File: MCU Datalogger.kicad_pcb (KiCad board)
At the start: 4 copper layers, 52.1 x 33 mm, 31 parts, among them J1 Conn_01x04_Pin, J2 Conn_01x09_Pin, J3 Conn_01x04_Pin, J4 Conn_02x03_Odd_Even, U1 DS1337S+, U2 24LC1025, U3 24LC1025, U4 ATMEGA328P-AU, Y1 32.768 KHz, Y2 16 MHz

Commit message: Minor changes.
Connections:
- net Net-(U4-AREF) renamed /Abc123
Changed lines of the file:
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@@
 	(net 3 "Net-(U4-PB6)")
 	(net 4 "Net-(U4-PB7)")
-	(net 5 "Net-(U4-AREF)")
+	(net 5 "/Abc123")
 	(net 6 "/SCK")
 	(net 7 "Net-(D1-K)")
@@
 			(layers "F.Cu" "F.Paste" "F.Mask")
 			(roundrect_rratio 0.25)
-			(net 5 "Net-(U4-AREF)")
+			(net 5 "/Abc123")
 			(pintype "passive")
 		)
@@
 			(size 1.5 0.55)
 			(layers "F.Cu" "F.Paste" "F.Mask")
-			(net 5 "Net-(U4-AREF)")
+			(net 5 "/Abc123")
 			(pinfunction "AREF")
 			(pintype "input")

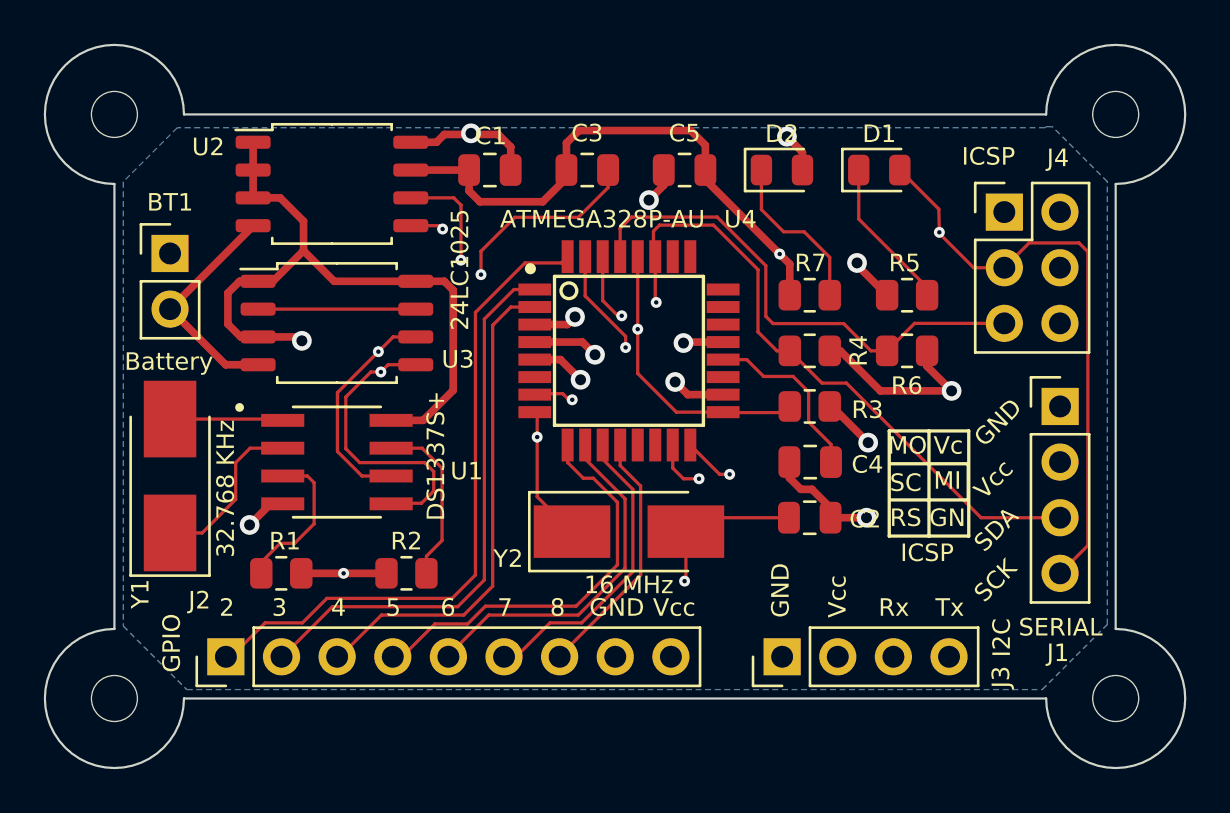
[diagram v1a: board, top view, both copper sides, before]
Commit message: Fixed issue with I2C SCL signal.
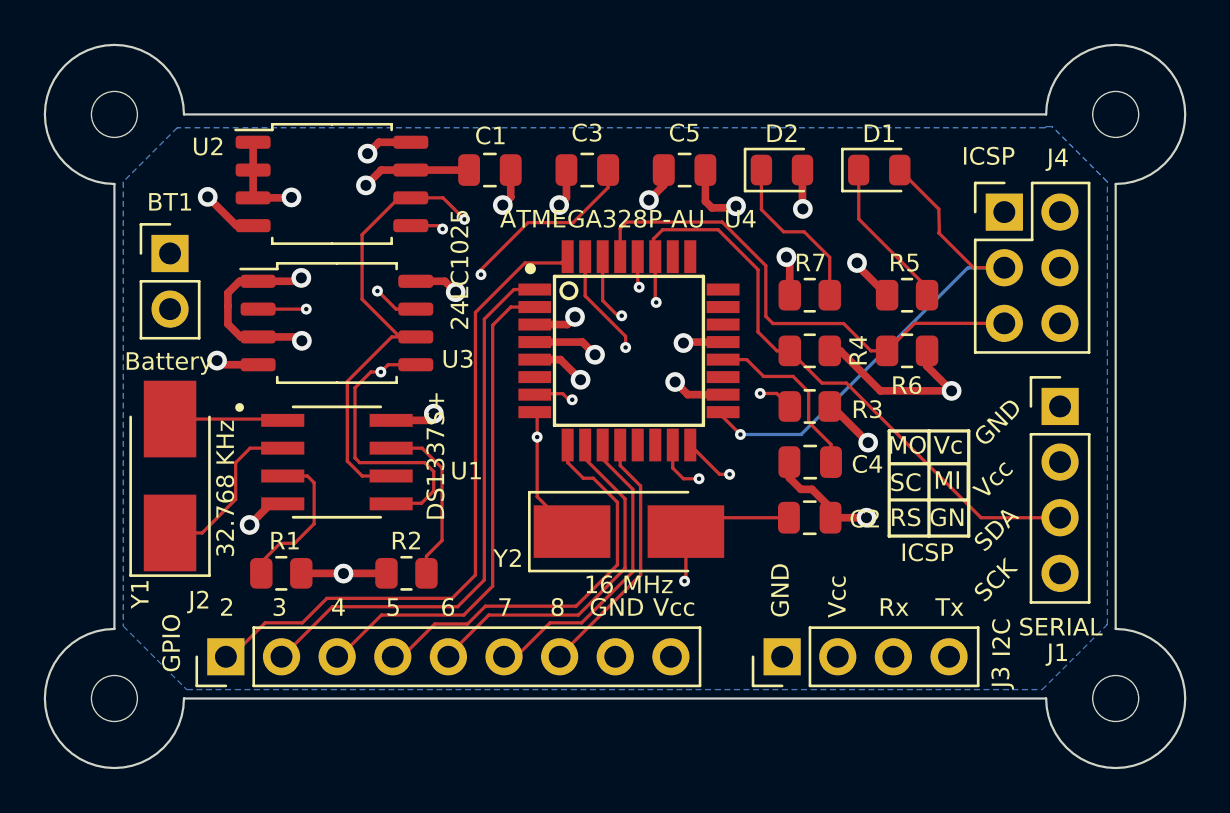
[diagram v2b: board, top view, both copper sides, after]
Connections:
- J1 pad 4: /SCK -> /SCL
- R3 pad 2: /SCK -> /SCL
- U1 pad 6: /SCK -> /SCL
- U2 pad 6: /SCK -> /SCL
- U3 pad 6: /SCK -> /SCL
- U4 pad 28: /SCK -> /SCL
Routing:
- net /SCK: track 88.7 -> 23.8 mm, vias 4 -> 1
- net /SCL: track 0.00 -> 59.2 mm, vias 0 -> 3
- net GND: track 51.8 -> 31.6 mm, vias 7 -> 12
- net /Vcc: track 61.4 -> 44.9 mm, vias 9 -> 14
- net /SDA: track 64.9 -> 64.2 mm
- net Net-(U3-A1): track 7.20 -> 7.90 mm, vias 0 -> 2
